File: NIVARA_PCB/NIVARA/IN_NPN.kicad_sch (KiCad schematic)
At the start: 0 parts

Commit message: avance en diagramas
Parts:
- added C6: C_0603, PCM_Capacitor_SMD_AKL:C_0603_1608Metric, symbol PCM_Capacitor_AKL:C_0603
- added R3, R4, R5, R6: ?, PCM_Resistor_SMD_AKL:R_0603_1608Metric, symbol PCM_Resistor_AKL:R_0603
- added TP2: TestPoint, symbol Connector:TestPoint
- added U2: PC817, PCM_Package_DIP_AKL:DIP-4_W7.62mm_SMDSocket_SmallPads, symbol Isolator:PC817
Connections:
- new net: C6.1, R5.2, R6.2, TP2.1, U2.4
- new net: R4.1, U2.2
- new net: R3.1, U2.1
- new net +3V3: R5.1, R6.1
- new net GND: C6.2, U2.3

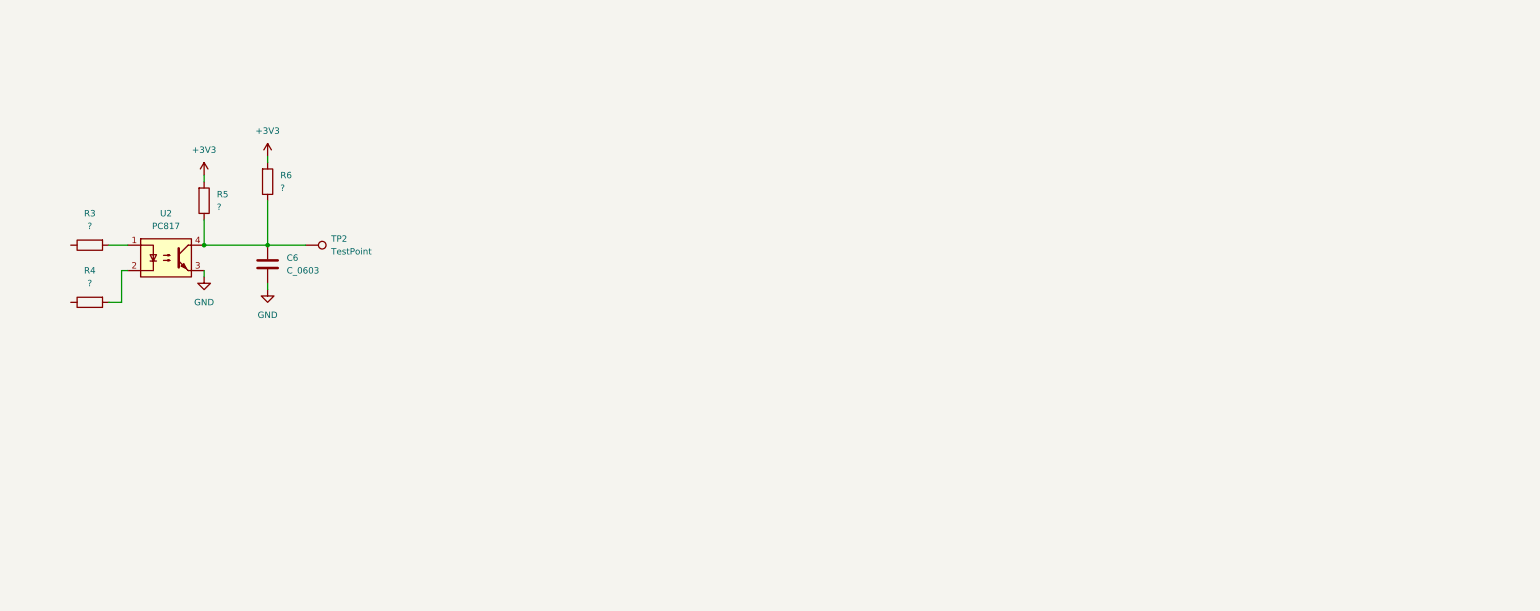
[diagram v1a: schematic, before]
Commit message: AVANCES
se realizaron avances con las entradas NPN, PNP. tambien se realizaron avances con las salidas de RELAYS
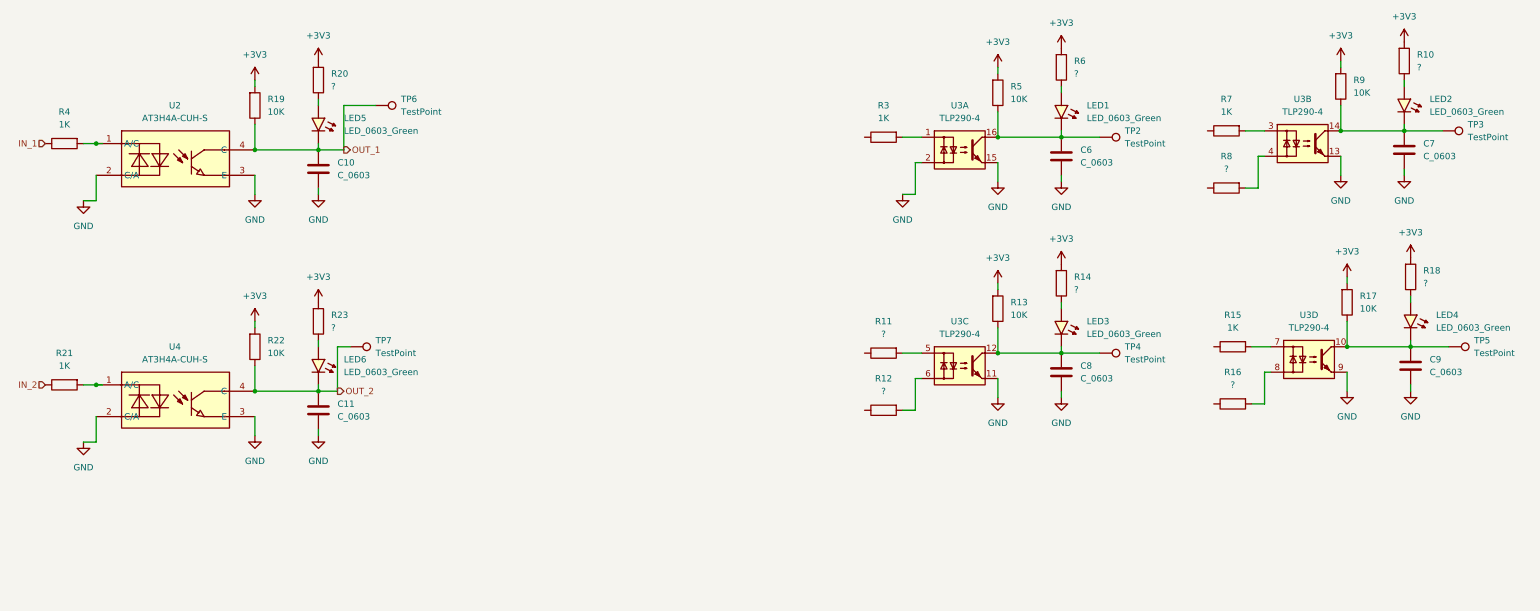
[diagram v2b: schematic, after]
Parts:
- removed U2: PC817, PCM_Package_DIP_AKL:DIP-4_W7.62mm_SMDSocket_SmallPads, symbol Isolator:PC817
- added C10, C11, C7, C8, C9: C_0603, PCM_Capacitor_SMD_AKL:C_0603_1608Metric, symbol PCM_Capacitor_AKL:C_0603
- added LED1, LED2, LED3, LED4, LED5, LED6: LED_0603_Green, PCM_LED_SMD_AKL:LED_0603_1608Metric, symbol PCM_LED_AKL:LED_0603_Green
- added R10, R11, R12, R14, R16, R18, R20, R23, R8: ?, PCM_Resistor_SMD_AKL:R_0603_1608Metric, symbol PCM_Resistor_AKL:R_0603
- added R13, R17, R19, R22, R9: 10K, PCM_Resistor_SMD_AKL:R_0603_1608Metric, symbol PCM_Resistor_AKL:R_0603
- added R15, R21, R7: 1K, PCM_Resistor_SMD_AKL:R_0603_1608Metric, symbol PCM_Resistor_AKL:R_0603
- added TP3, TP4, TP5, TP6, TP7: TestPoint, symbol Connector:TestPoint
- added U2, U4: AT3H4A-CUH-S, easyeda2kicad:SSOP-4_L2.7-W4.6-P1.27-LS7.0-TL, symbol easyeda2kicad:AT3H4A-CUH-S
- added U3: TLP290-4, Package_SO:SOP-16_4.55x10.3mm_P1.27mm, symbol Isolator:TLP290-4
- R3, R4: value ? -> 1K
- R5: value ? -> 10K
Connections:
- net +3V3: now also R10.1, R13.1, R14.1, R17.1, R18.1, R19.1, R20.1, R22.1, R23.1, R9.1
- net GND: now also C10.2, C11.2, C7.2, C8.2, C9.2, U2.2 (C/A), U2.3 (E), U3.11, U3.13, U3.15, U3.2, U3.9, U4.2 (C/A), U4.3 (E)
- net at C6.1, R5.2, TP2.1: now also LED1.1 (K), U3.16; no longer R6.2
- net at R4.1: now also U2.1 (A/C)
- net IN_1: now reaches R4.2
- net at R3.1: now also U3.1
- new net: C7.1, LED2.1 (K), R9.2, TP3.1, U3.14
- new net: LED1.2 (A), R6.2
- new net: LED6.2 (A), R23.2
- new net: LED3.2 (A), R14.2
- new net: LED5.2 (A), R20.2
- new net: R21.1, U4.1 (A/C)
- new net: C8.1, LED3.1 (K), R13.2, TP4.1, U3.12
- new net: C9.1, LED4.1 (K), R17.2, TP5.1, U3.10
- new net: LED4.2 (A), R18.2
- new net: LED2.2 (A), R10.2
- new net: R15.1, U3.7
- new net: R7.1, U3.3
- new net: R8.1, U3.4
- new net: R16.1, U3.8
- new net: R11.1, U3.5
- new net: R12.1, U3.6
- new net IN_2: R21.2
- new net OUT_1: C10.1, LED5.1 (K), R19.2, TP6.1, U2.4 (C)
- new net OUT_2: C11.1, LED6.1 (K), R22.2, TP7.1, U4.4 (C)
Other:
- moved on the sheet: C6, R3, R5, R6, TP2

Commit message: se agregaron partnumbers
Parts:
- U2, U4: PART NUMBERT (none) -> AT3H4A-CUH-S
- U3: PART NUMBERT (none) -> TLP290-4(GB-TP,E(T
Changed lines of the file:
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@@
 			)
 		)
-		(property "PART NUMBERT" ""
+		(property "PART NUMBERT" "AT3H4A-CUH-S"
 			(at 44.45 43.18 0)
 			(effects
@@
 			)
 		)
-		(property "PART NUMBERT" ""
+		(property "PART NUMBERT" "AT3H4A-CUH-S"
 			(at 44.45 91.44 0)
 			(effects
@@
 			)
 		)
-		(property "PART NUMBERT" ""
+		(property "PART NUMBERT" "TLP290-4(GB-TP,E(T"
 			(at 269.24 39.37 0)
 			(effects
@@
 			)
 		)
-		(property "PART NUMBERT" ""
+		(property "PART NUMBERT" "TLP290-4(GB-TP,E(T"
 			(at 270.51 82.55 0)
 			(effects
@@
 			)
 		)
-		(property "PART NUMBERT" ""
+		(property "PART NUMBERT" "TLP290-4(GB-TP,E(T"
 			(at 200.66 40.64 0)
 			(effects
@@
 			)
 		)
-		(property "PART NUMBERT" ""
+		(property "PART NUMBERT" "TLP290-4(GB-TP,E(T"
 			(at 200.66 83.82 0)
 			(effects

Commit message: RS_485 ADD MODULE
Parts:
- R21, R4: footprint PCM_Resistor_SMD_AKL:R_0603_1608Metric -> PCM_Resistor_SMD_AKL:R_1206_3216Metric_Pad1.30x1.75mm_HandSolder; PART NUMBERT (none) -> CRCW12061K00FKEAHP

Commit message: ACTUALIZACION
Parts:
- removed C6, C7, C8, C9: C_0603, PCM_Capacitor_SMD_AKL:C_0603_1608Metric, symbol PCM_Capacitor_AKL:C_0603
- removed LED1, LED2, LED3, LED4: LED_0603_Green, PCM_LED_SMD_AKL:LED_0603_1608Metric, symbol PCM_LED_AKL:LED_0603_Green
- removed R10, R11, R12, R14, R16, R18, R6, R8: ?, PCM_Resistor_SMD_AKL:R_0603_1608Metric, symbol PCM_Resistor_AKL:R_0603
- removed R13, R17, R5, R9: 10K, PCM_Resistor_SMD_AKL:R_0603_1608Metric, symbol PCM_Resistor_AKL:R_0603
- removed R15, R3, R7: 1K, PCM_Resistor_SMD_AKL:R_0603_1608Metric, symbol PCM_Resistor_AKL:R_0603
- removed TP2, TP3, TP4, TP5: TestPoint, symbol Connector:TestPoint
- removed U3: TLP290-4, Package_SO:SOP-16_4.55x10.3mm_P1.27mm, symbol Isolator:TLP290-4
- TP6, TP7: footprint (none) -> TestPoint:TestPoint_THTPad_D1.0mm_Drill0.5mm
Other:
- moved on the sheet: C10, C11, LED5, LED6, R19, R20, R21, R22, R23, R4, TP6, TP7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

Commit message: avance
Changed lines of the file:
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@@
-	)
-	(junction
-		(at 119.38 64.77)
-		(diameter 0)
-		(color 0 0 0 0)
 	)
 	(junction
@@
 		(color 0 0 0 0)
 	)
-	(junction
-		(at 119.38 113.03)
-		(diameter 0)
-		(color 0 0 0 0)
-	)
 	(wire
 		(pts
 			(xy 163.83 123.19) (xy 163.83 121.92)
-		)
-		(stroke
-			(width 0)
-			(type default)
-		)
-	)
-	(wire
-		(pts
-			(xy 119.38 64.77) (xy 120.65 64.77)
 		)
 		(stroke
@@
 	(wire
 		(pts
-			(xy 116.84 113.03) (xy 119.38 113.03)
-		)
-		(stroke
-			(width 0)
-			(type default)
-		)
-	)
-	(wire
-		(pts
 			(xy 151.13 52.07) (xy 151.13 53.34)
 		)
@@
 		(pts
 			(xy 151.13 74.93) (xy 151.13 71.12)
-		)
-		(stroke
-			(width 0)
-			(type default)
-		)
-	)
-	(wire
-		(pts
-			(xy 119.38 113.03) (xy 120.65 113.03)
 		)
 		(stroke
@@
 		)
 		(stroke
+			(width 0)
+			(type default)
+		)
+	)
+	(wire
+		(pts
+			(xy 116.84 113.03) (xy 119.38 113.03)
+		)
+		(stroke

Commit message: SALIDAS DE VOLTAJE Y CORRIENTE
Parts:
- C10, C11: value C_0603 -> 1uF; PART NUMBERT (none) -> CL10A105KB8NNNC
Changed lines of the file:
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@@
 			)
 		)
-		(property "Value" "C_0603"
+		(property "Value" "1uF"
 			(at 167.64 119.3799 0)
 			(effects
@@
 			)
 		)
-		(property "PART NUMBERT" ""
+		(property "PART NUMBERT" "CL10A105KB8NNNC"
 			(at 163.83 118.11 0)
 			(effects
@@
 			)
 		)
-		(property "Value" "C_0603"
+		(property "Value" "1uF"
 			(at 167.64 71.1199 0)
 			(effects
@@
 			)
 		)
-		(property "PART NUMBERT" ""
+		(property "PART NUMBERT" "CL10A105KB8NNNC"
 			(at 163.83 69.85 0)
 			(effects

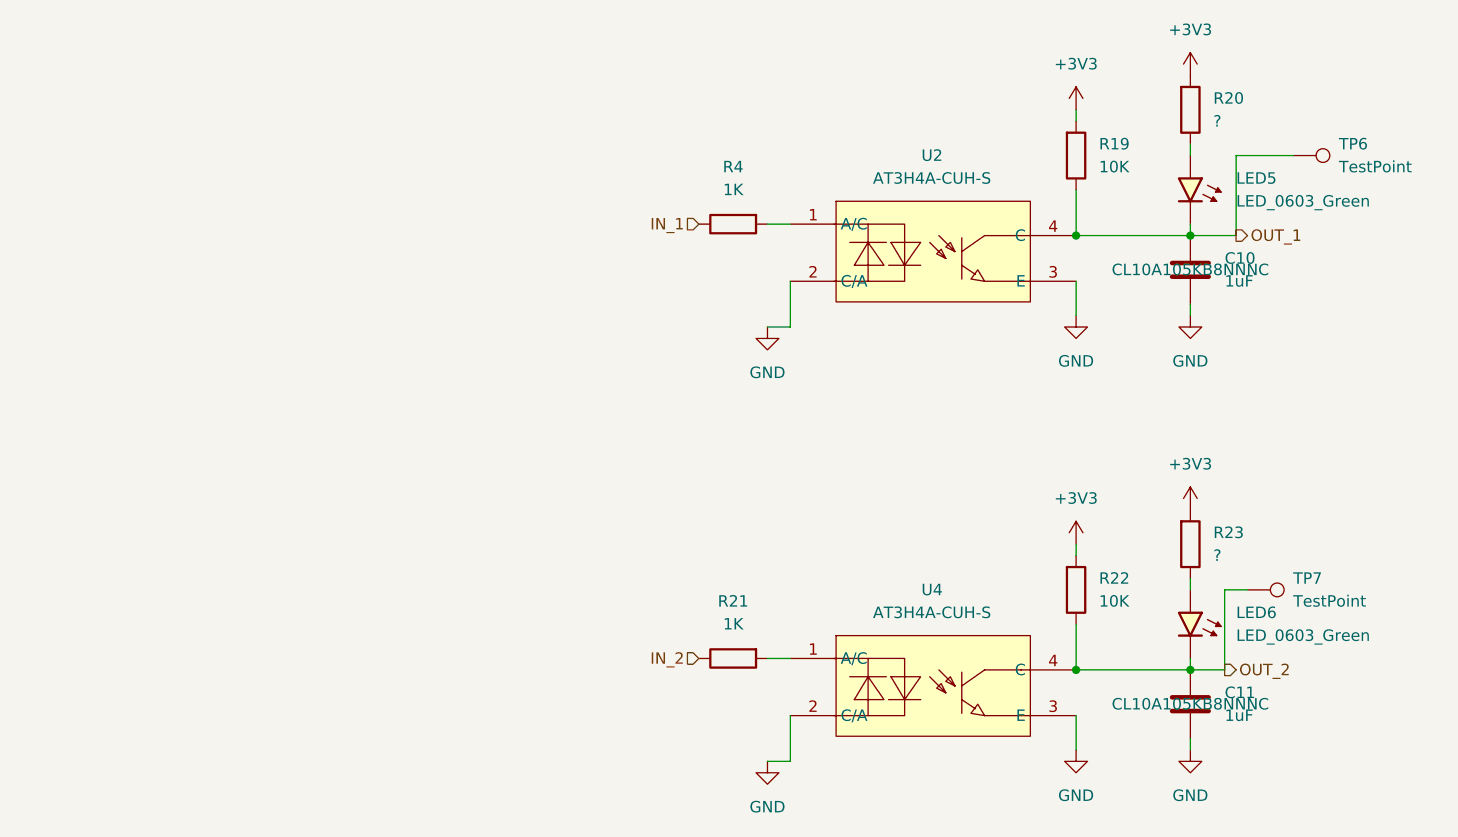
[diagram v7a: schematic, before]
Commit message: Se organizaron componentes en el area de PCB
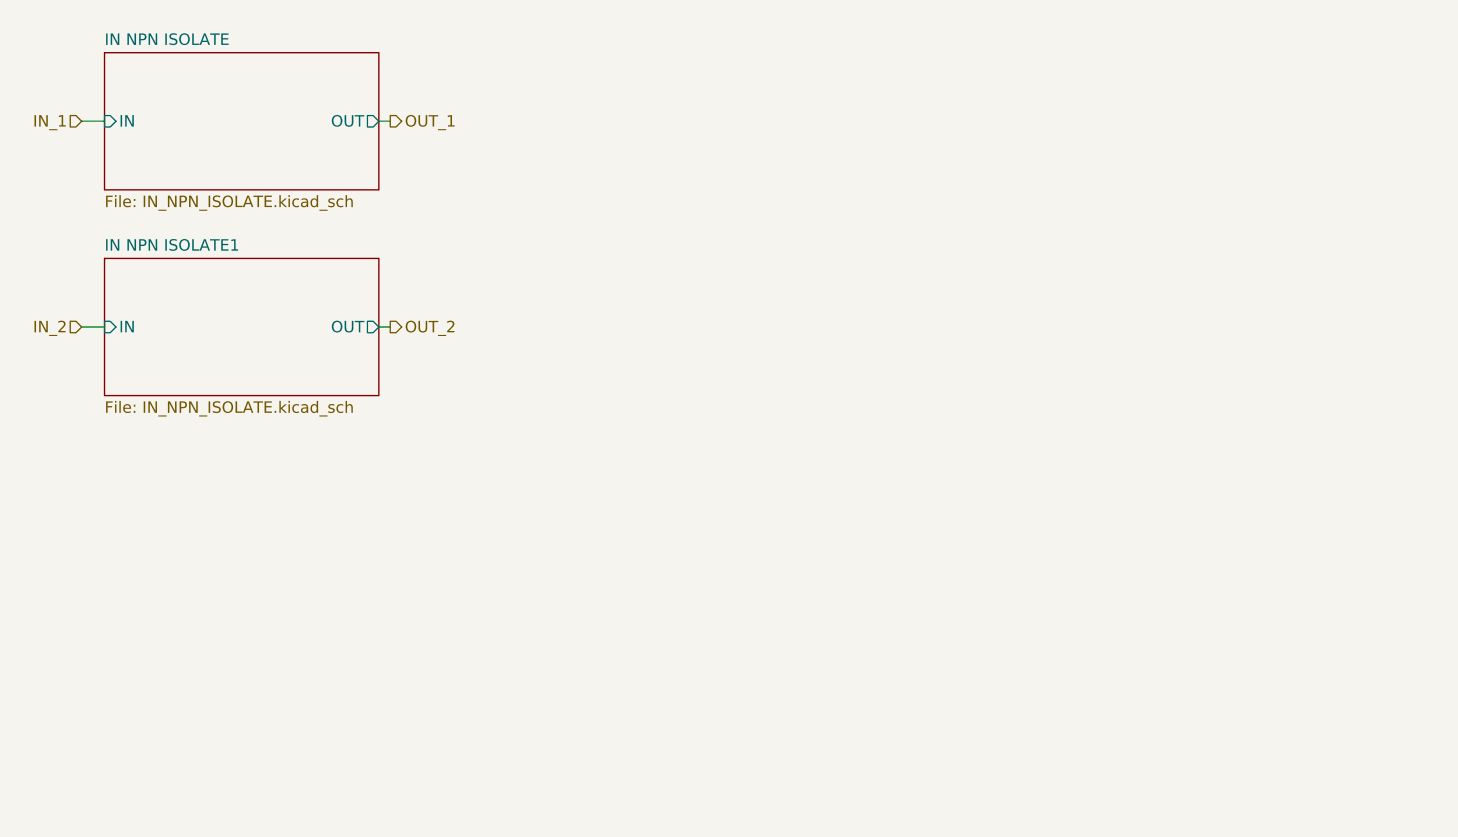
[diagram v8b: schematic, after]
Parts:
- removed C10, C11: 1uF, PCM_Capacitor_SMD_AKL:C_0603_1608Metric, symbol PCM_Capacitor_AKL:C_0603
- removed LED5, LED6: LED_0603_Green, PCM_LED_SMD_AKL:LED_0603_1608Metric, symbol PCM_LED_AKL:LED_0603_Green
- removed R19, R22: 10K, PCM_Resistor_SMD_AKL:R_0603_1608Metric, symbol PCM_Resistor_AKL:R_0603
- removed R20, R23: ?, PCM_Resistor_SMD_AKL:R_0603_1608Metric, symbol PCM_Resistor_AKL:R_0603
- removed R21, R4: 1K, PCM_Resistor_SMD_AKL:R_1206_3216Metric_Pad1.30x1.75mm_HandSolder, symbol PCM_Resistor_AKL:R_0603
- removed TP6, TP7: TestPoint, TestPoint:TestPoint_THTPad_D1.0mm_Drill0.5mm, symbol Connector:TestPoint
- removed U2, U4: AT3H4A-CUH-S, easyeda2kicad:SSOP-4_L2.7-W4.6-P1.27-LS7.0-TL, symbol easyeda2kicad:AT3H4A-CUH-S
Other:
- added sheet IN NPN ISOLATE (IN_NPN_ISOLATE.kicad_sch)
- added sheet IN NPN ISOLATE1 (IN_NPN_ISOLATE.kicad_sch)
